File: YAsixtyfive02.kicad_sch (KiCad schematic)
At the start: 58 parts, among them J1 ~{NMI}, J2 Aux 5VDC, J3 Power 5V, J4 Expansion Bus, J7 GND, J8 FTDI Serial2USB, SW1 RESET, SW2 SW_Push_DPDT, U1 WD65C02, U10 74LS138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

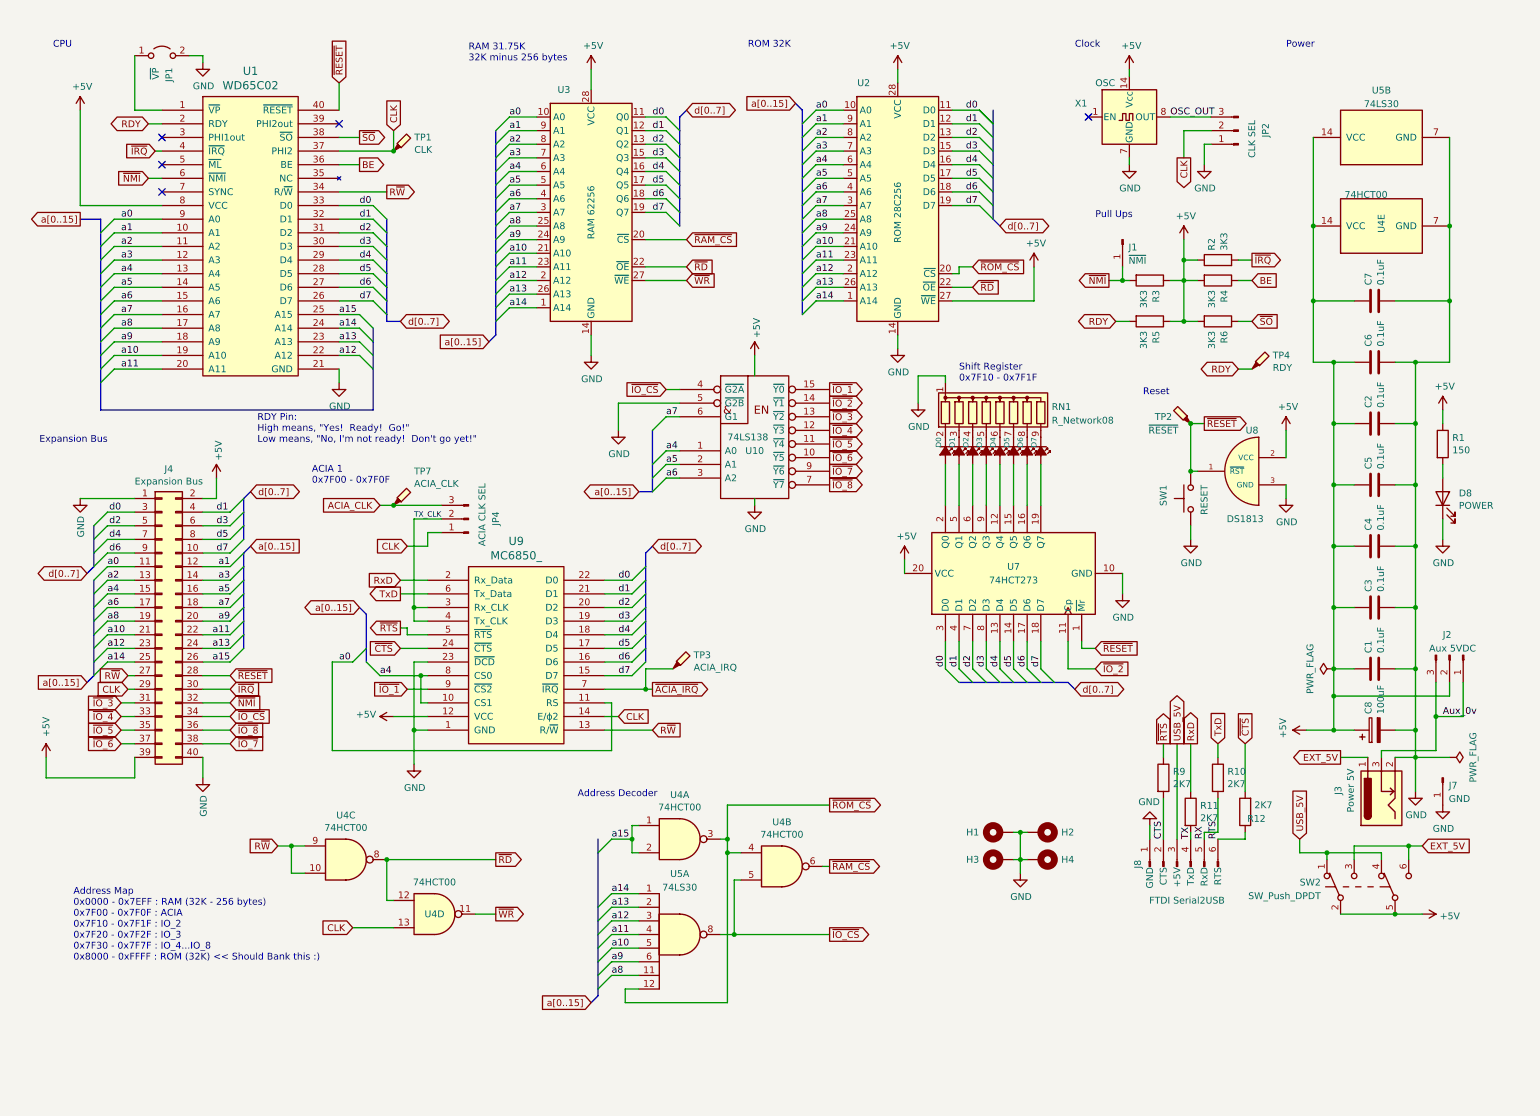
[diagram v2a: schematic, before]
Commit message: cleaned up schematic
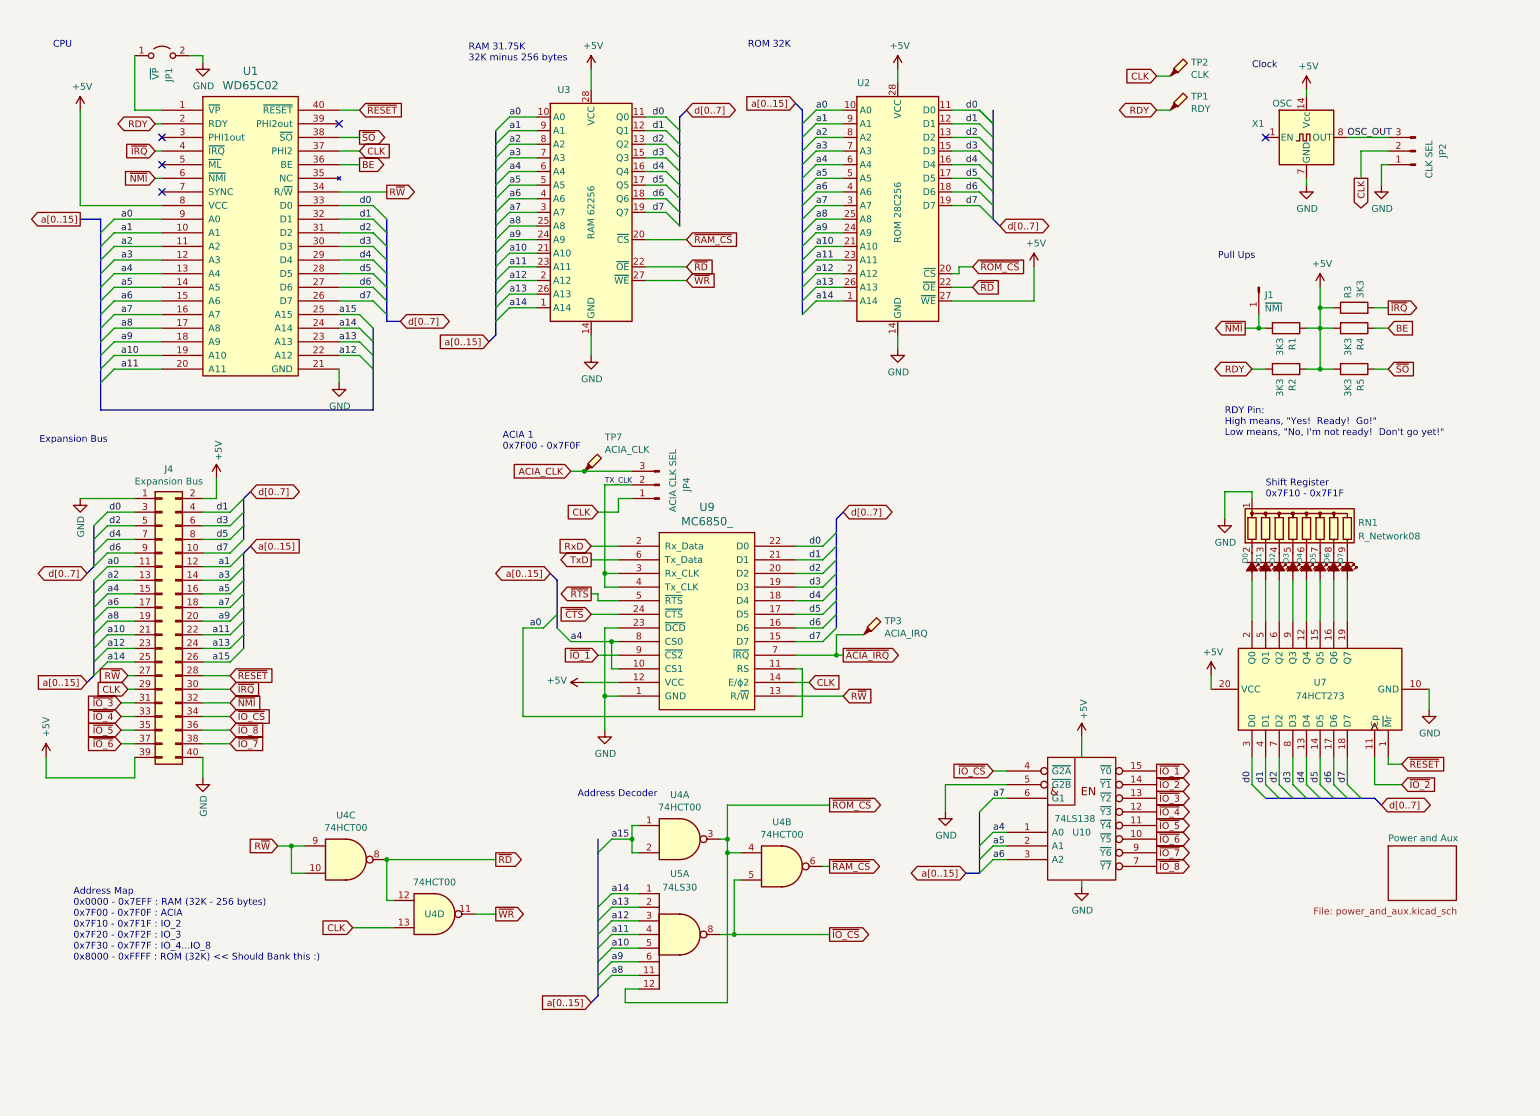
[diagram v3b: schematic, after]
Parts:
- removed C1, C2, C3, C4, C5, C6, C7: 0.1uF, Capacitor_THT:C_Disc_D4.3mm_W1.9mm_P5.00mm, symbol Device:C
- removed C8: 100uF, Capacitor_THT:CP_Radial_D6.3mm_P2.50mm, symbol YAsixtyfive02-rescue:CP-Device
- removed D8: POWER, LED_THT:LED_D3.0mm, symbol Device:LED
- removed H1, H2, H3, H4: MNT, MountingHole:MountingHole_3.2mm_M3_DIN965_Pad_TopBottom, symbol Mechanical:MountingHole_Pad
- removed J2: Aux 5VDC, Connector_PinHeader_2.54mm:PinHeader_1x03_P2.54mm_Vertical, symbol Connector:Conn_01x03_Male
- removed J3: Power 5V, Connector_BarrelJack:BarrelJack_Horizontal, symbol Connector:Barrel_Jack_Switch
- removed J7: GND, Connector_PinHeader_2.54mm:PinHeader_1x01_P2.54mm_Vertical, symbol Connector:Conn_01x01_Male
- removed J8: FTDI Serial2USB, Connector_PinHeader_2.54mm:PinHeader_1x06_P2.54mm_Vertical, symbol YAsixtyfive02-rescue:FTDI_Conn_01x06_Male-Connector
- removed R10, R11, R12, R9: 2K7, Resistor_THT:R_Axial_DIN0207_L6.3mm_D2.5mm_P10.16mm_Horizontal, symbol Device:R
- removed R6: 3K3, Resistor_THT:R_Axial_DIN0207_L6.3mm_D2.5mm_P10.16mm_Horizontal, symbol Device:R
- removed SW1: RESET, Button_Switch_THT:SW_PUSH_6mm_H5mm, symbol Switch:SW_Push
- removed SW2: SW_Push_DPDT, Button_Switch_THT:SW_NKK_GW12LJP, symbol Switch:SW_Push_DPDT
- removed TP4: RDY, TestPoint:TestPoint_THTPad_1.0x1.0mm_Drill0.5mm, symbol Connector:TestPoint_Probe
- removed unit 5 of U4
- removed unit 2 of U5
- removed U8: DS1813, Package_TO_SOT_THT:TO-92, symbol YAsixtyfive02-rescue:DS1813-10-DS1813-10
- R1: value 150 -> 3K3
- TP1: value CLK -> RDY; footprint TestPoint:TestPoint_THTPad_1.5x1.5mm_Drill0.7mm -> TestPoint:TestPoint_THTPad_1.0x1.0mm_Drill0.5mm
- TP2: value ~{RESET} -> CLK
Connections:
- net +5V: now also R5.2; no longer R5.1
- net CLK: now also TP2.1; no longer TP1.1
- net RDY: now also R2.2, TP1.1; no longer R5.2
- net ~{IRQ}: now also R3.2; no longer R2.2
- net ~{NMI}: now also R1.2; no longer R3.2
- net ~{RESET}: no longer TP2.1
- net ~{SO}: now also R5.1
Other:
- added sheet Power and Aux (power_and_aux.kicad_sch)
- note removed: "Power"
- note removed: "Reset"
- moved on the sheet: D0, D1, D2, D3, D4, D5, D6, D7, JP2, JP4, RN1, TP3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

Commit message: Schematic re-organized
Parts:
- removed J4: Expansion Bus, Connector_PinSocket_2.54mm:PinSocket_2x20_P2.54mm_Vertical, symbol Connector_Generic:Conn_02x20_Odd_Even
- removed JP2: CLK SEL, Connector_PinHeader_2.54mm:PinHeader_1x03_P2.54mm_Vertical, symbol Connector:Conn_01x03_Male
- removed JP4: ACIA CLK SEL, Connector_PinHeader_2.54mm:PinHeader_1x03_P2.54mm_Vertical, symbol Connector:Conn_01x03_Male
- removed TP1: RDY, TestPoint:TestPoint_THTPad_1.0x1.0mm_Drill0.5mm, symbol Connector:TestPoint_Probe
- removed TP2: CLK, TestPoint:TestPoint_THTPad_1.5x1.5mm_Drill0.7mm, symbol Connector:TestPoint_Probe
- removed TP3: ACIA_IRQ, TestPoint:TestPoint_THTPad_1.0x1.0mm_Drill0.5mm, symbol Connector:TestPoint_Probe
- removed TP7: ACIA_CLK, TestPoint:TestPoint_THTPad_1.5x1.5mm_Drill0.7mm, symbol Connector:TestPoint_Probe
- removed X1: OSC, Oscillator:Oscillator_DIP-14, symbol Oscillator:CXO_DIP14
- added JP3: ACIA CLK SEL, Connector_PinHeader_2.54mm:PinHeader_1x03_P2.54mm_Vertical, symbol Connector:Conn_01x03_Male
- renumbered R3 to R2, R1 to R3, R2 to R5, R5 to R6
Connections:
- net ACIA_CLK: now also JP3.3 (Pin_3)
- net CLK: now also JP3.1 (Pin_1)
- net TX_CLK: now also JP3.2 (Pin_2)
- no-connect marks 5 -> 4
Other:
- note added: "Bank Latch 0x7F10 - 0x7F1F"
- note removed: "Clock"
- note removed: "Expansion Bus"
- note removed: "Shift Register 0x7F10 - 0x7F1F"
- moved on the sheet: D0, D1, D2, D3, D4, D5, D6, D7, J1, R2, R3, R4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

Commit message: Schematic and PCB Updated
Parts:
- renumbered JP3 to JP4
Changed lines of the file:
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@@
   (symbol (lib_id "Connector:Conn_01x03_Male") (at 143.51 88.9 180) (unit 1)
     (in_bom yes) (on_board yes)
-    (property "Reference" "JP3" (id 0) (at 148.59 90.17 90)
+    (property "Reference" "JP4" (id 0) (at 148.59 90.17 90)
       (effects (font (size 1.27 1.27)) (justify right))
     )
@@
       (reference "J1") (unit 1) (value "~{NMI}") (footprint "Connector_PinHeader_2.54mm:PinHeader_1x01_P2.54mm_Vertical")
     )
-    (path "/2f707a14-2b5c-4a52-8408-8f4926d12582/0b79242b-1c36-455b-b596-ca1b42f87b16"
-      (reference "J2") (unit 1) (value "GND") (footprint "Connector_PinHeader_2.54mm:PinHeader_1x01_P2.54mm_Vertical")
-    )
     (path "/2f707a14-2b5c-4a52-8408-8f4926d12582/07015d73-0310-4851-9b16-bc3559f3f1e8"
-      (reference "J3") (unit 1) (value "Aux 5VDC") (footprint "Connector_PinHeader_2.54mm:PinHeader_1x03_P2.54mm_Vertical")
+      (reference "J2") (unit 1) (value "AUX 5VDC") (footprint "Connector_PinHeader_2.54mm:PinHeader_1x03_P2.54mm_Vertical")
+    )
+    (path "/2f707a14-2b5c-4a52-8408-8f4926d12582/8f296b62-1060-48e7-a2d1-f25a3e2fc63b"
+      (reference "J3") (unit 1) (value "Power 5V") (footprint "Connector_BarrelJack:BarrelJack_Horizontal")
     )
     (path "/2f707a14-2b5c-4a52-8408-8f4926d12582/cb3dfdbe-0707-4d8c-bd32-febd6074bb18"
       (reference "J4") (unit 1) (value "Expansion Bus") (footprint "Connector_PinSocket_2.54mm:PinSocket_2x20_P2.54mm_Vertical")
     )
-    (path "/2f707a14-2b5c-4a52-8408-8f4926d12582/8f296b62-1060-48e7-a2d1-f25a3e2fc63b"
-      (reference "J5") (unit 1) (value "Power 5V") (footprint "Connector_BarrelJack:BarrelJack_Horizontal")
-    )
     (path "/2f707a14-2b5c-4a52-8408-8f4926d12582/1a87ef41-cb18-4c6d-8f9a-e4cb13e15948"
       (reference "J6") (unit 1) (value "FTDI Serial2USB") (footprint "Connector_PinHeader_2.54mm:PinHeader_1x06_P2.54mm_Vertical")
     )
+    (path "/2f707a14-2b5c-4a52-8408-8f4926d12582/0b79242b-1c36-455b-b596-ca1b42f87b16"
+      (reference "J7") (unit 1) (value "GND") (footprint "Connector_PinHeader_2.54mm:PinHeader_1x01_P2.54mm_Vertical")
+    )
     (path "/00000000-0000-0000-0000-000061231812"
       (reference "JP1") (unit 1) (value "~{VP}") (footprint "Connector_PinHeader_2.54mm:PinHeader_1x02_P2.54mm_Vertical")
@@
     )
     (path "/3b98ffc1-9035-4307-8f19-9251da72e25d"
-      (reference "JP3") (unit 1) (value "ACIA CLK SEL") (footprint "Connector_PinHeader_2.54mm:PinHeader_1x03_P2.54mm_Vertical")
+      (reference "JP4") (unit 1) (value "ACIA CLK SEL") (footprint "Connector_PinHeader_2.54mm:PinHeader_1x03_P2.54mm_Vertical")
+    )
+    (path "/2f707a14-2b5c-4a52-8408-8f4926d12582/ec82d084-09a9-463c-8f00-34fa8e6ff5bf"
+      (reference "R1") (unit 1) (value "150") (footprint "Resistor_THT:R_Axial_DIN0207_L6.3mm_D2.5mm_P10.16mm_Horizontal")
     )
     (path "/9c6b044c-e41c-4671-afd3-aaae88279b51"
@@
       (reference "R5") (unit 1) (value "3K3") (footprint "Resistor_THT:R_Axial_DIN0207_L6.3mm_D2.5mm_P10.16mm_Horizontal")
     )
-    (path "/2f707a14-2b5c-4a52-8408-8f4926d12582/ec82d084-09a9-463c-8f00-34fa8e6ff5bf"
-      (reference "R6") (unit 1) (value "150") (footprint "Resistor_THT:R_Axial_DIN0207_L6.3mm_D2.5mm_P10.16mm_Horizontal")
-    )
     (path "/fc702c50-0c03-4152-874f-46b58b317ba5"
       (reference "R6") (unit 1) (value "3K3") (footprint "Resistor_THT:R_Axial_DIN0207_L6.3mm_D2.5mm_P10.16mm_Horizontal")
@@
       (reference "RN1") (unit 1) (value "R_Network08") (footprint "Resistor_THT:R_Array_SIP9")
     )
+    (path "/2f707a14-2b5c-4a52-8408-8f4926d12582/168c1ae0-4f8c-4148-bc08-de17e4277d12"
+      (reference "SW1") (unit 1) (value "RESET") (footprint "Button_Switch_THT:SW_PUSH_6mm_H5mm")
+    )
     (path "/2f707a14-2b5c-4a52-8408-8f4926d12582/05f29c0e-2c9e-49cb-9b41-3f25352869d6"
-      (reference "SW1") (unit 1) (value "Power SW") (footprint "Button_Switch_THT:SW_NKK_GW12LJP")
-    )
-    (path "/2f707a14-2b5c-4a52-8408-8f4926d12582/168c1ae0-4f8c-4148-bc08-de17e4277d12"
-      (reference "SW2") (unit 1) (value "RESET") (footprint "Button_Switch_THT:SW_PUSH_6mm_H5mm")
+      (reference "SW2") (unit 1) (value "Power SW") (footprint "Button_Switch_THT:SW_NKK_GW12LJP")
     )
     (path "/2f707a14-2b5c-4a52-8408-8f4926d12582/3136a088-7bfd-4246-aa13-6b45f10faf20"

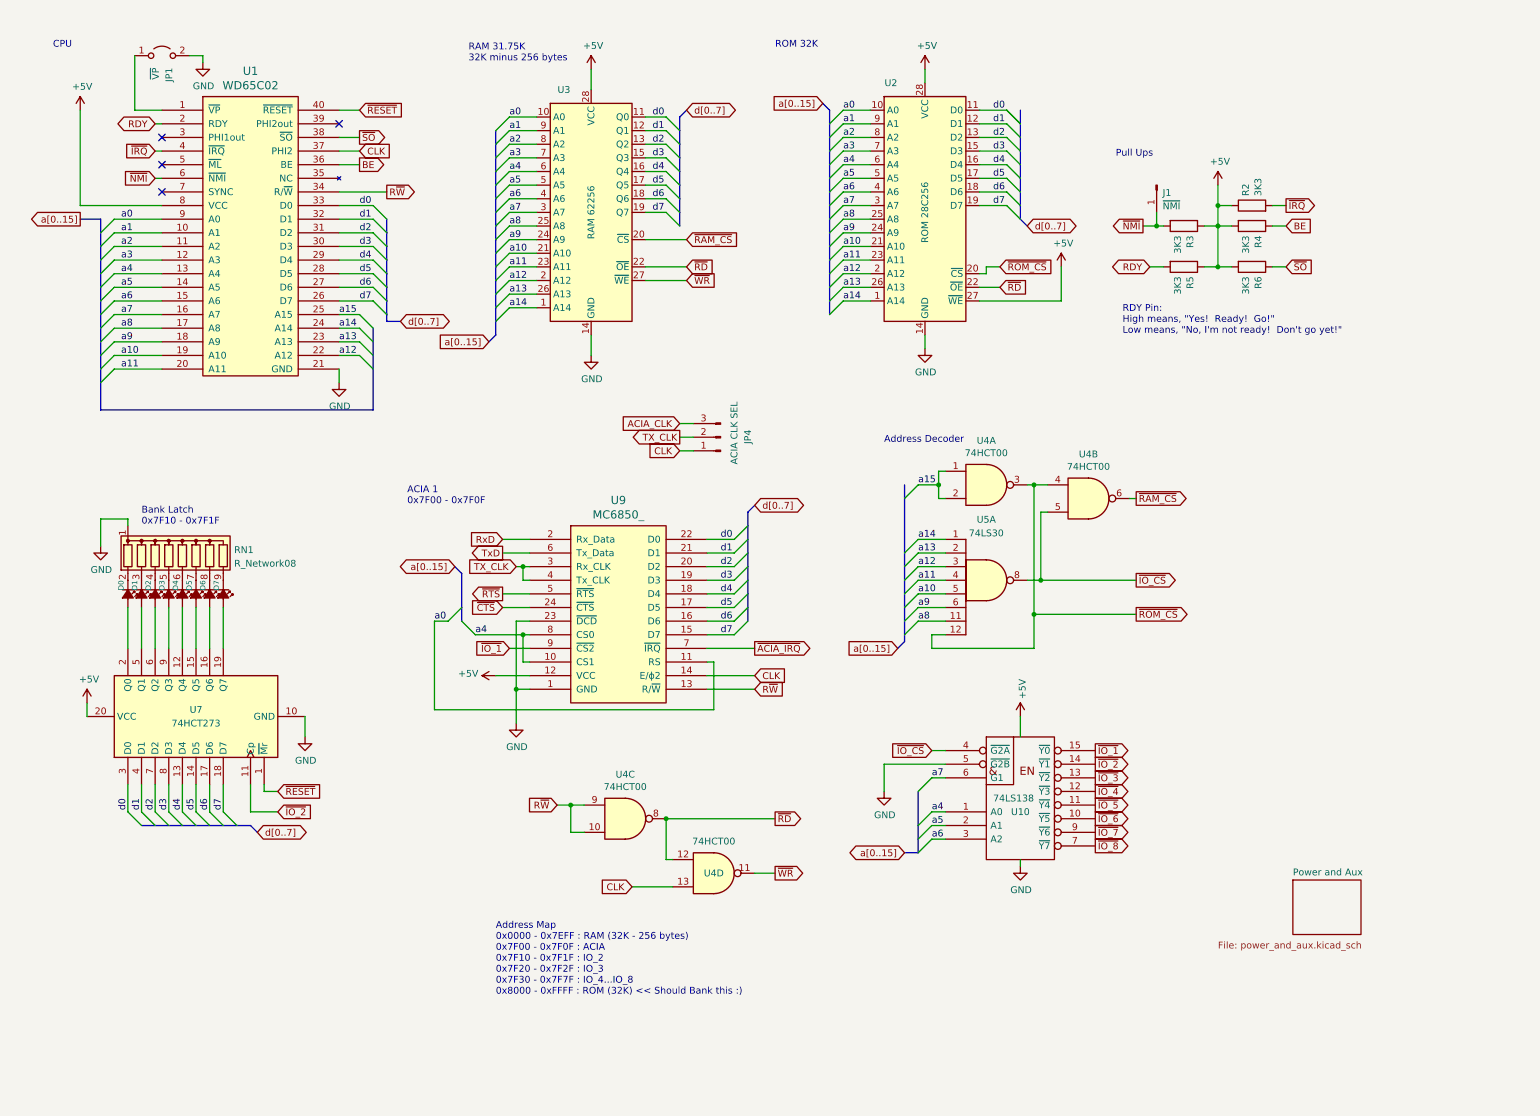
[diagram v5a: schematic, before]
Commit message: Added 6502 bus to schematic
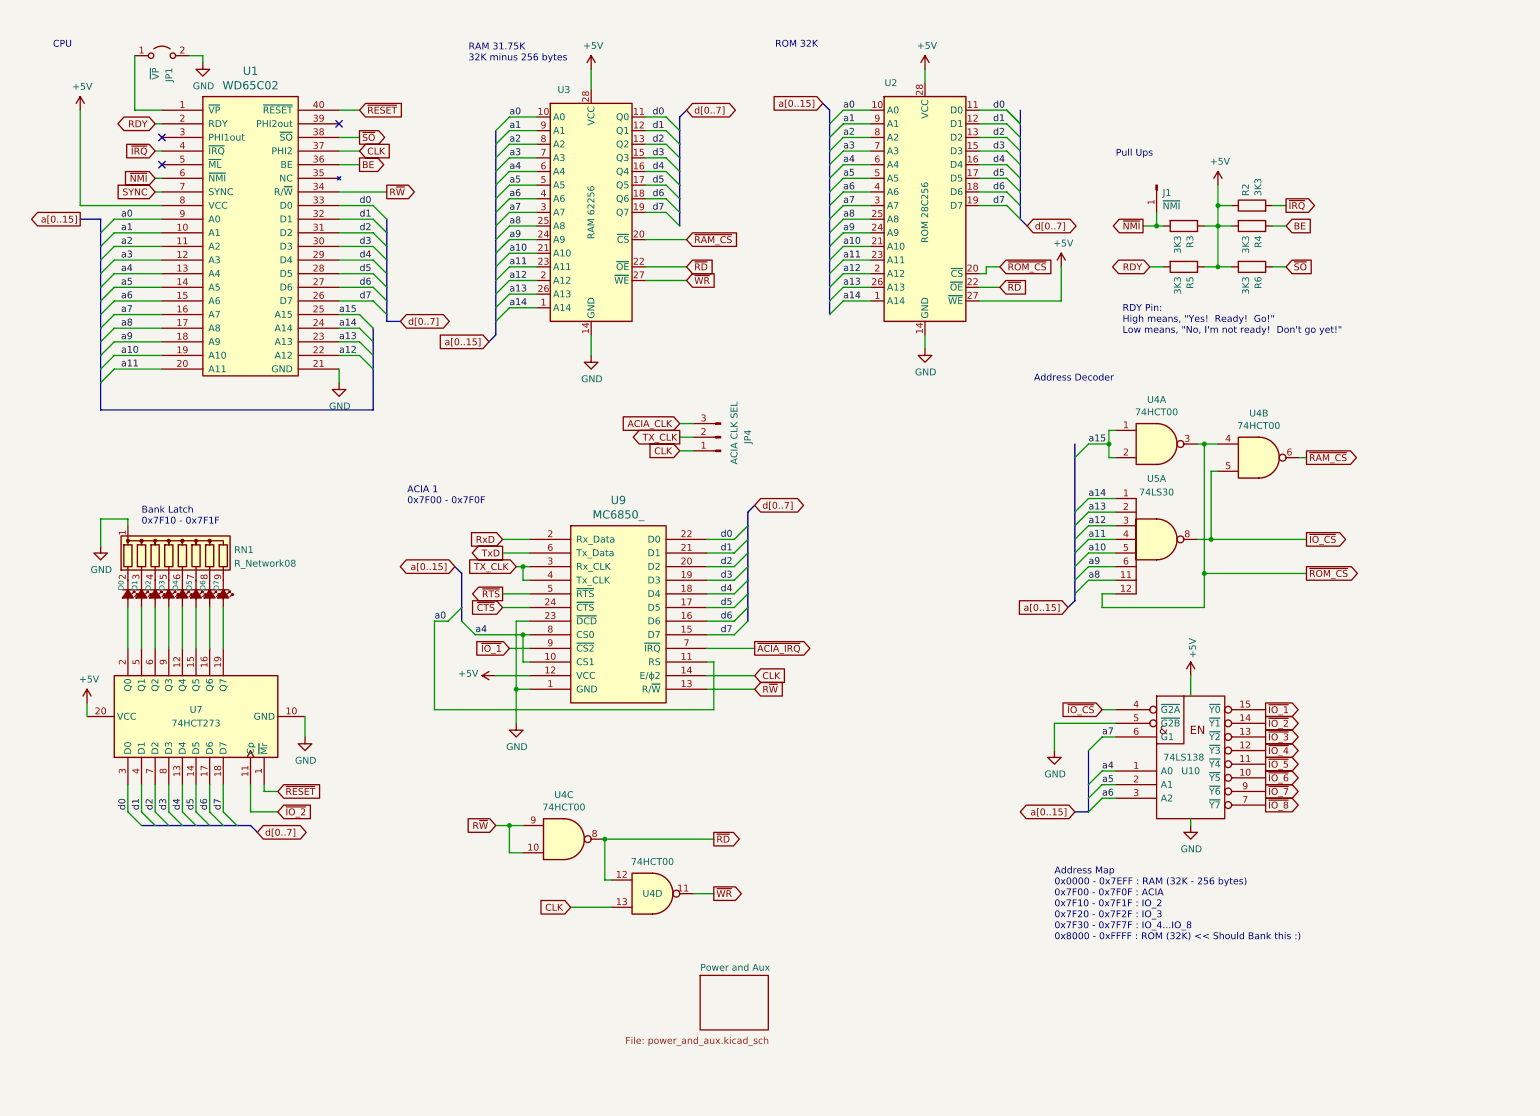
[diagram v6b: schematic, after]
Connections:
- net SYNC: now reaches U1.7 (SYNC)
- no-connect marks 4 -> 3
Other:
- moved on the sheet: U10, U4A, U4B, U4C, U4D, U5A
